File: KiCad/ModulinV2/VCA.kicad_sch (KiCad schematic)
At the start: 9 parts, among them IC12 AS3360D

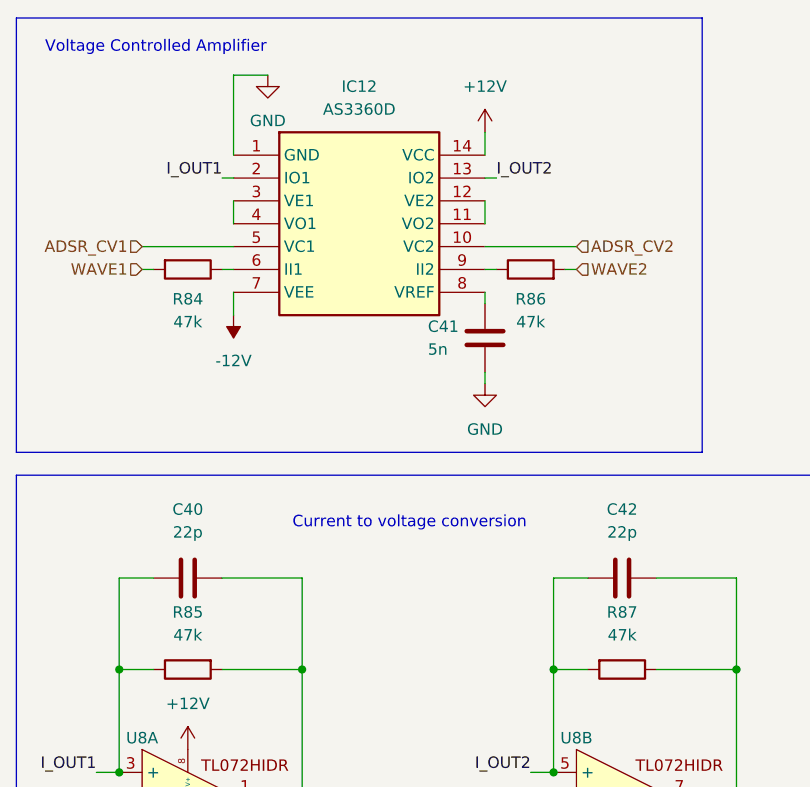
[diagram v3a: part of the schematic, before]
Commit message: Added initial power supply schematic and modified MCU components
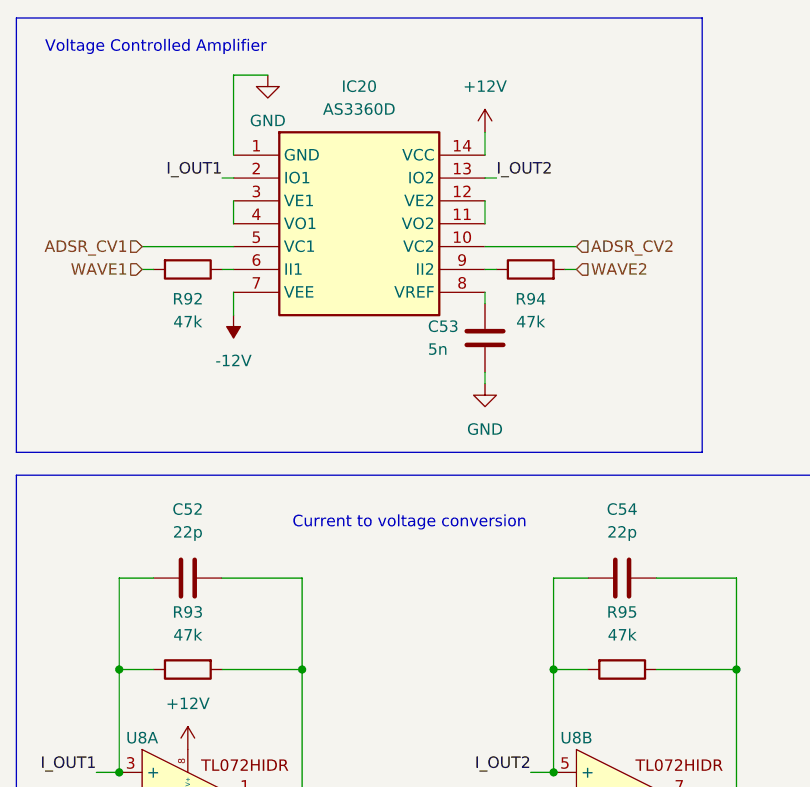
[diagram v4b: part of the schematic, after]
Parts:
- renumbered C40 to C52, C41 to C53, C42 to C54, IC12 to IC20, R84 to R92, R85 to R93, R86 to R94, R87 to R95
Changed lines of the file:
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@@
 		(dnp no)
 		(fields_autoplaced yes)
-		(property "Reference" "R87"
+		(property "Reference" "R95"
 			(at 81.28 80.01 90)
 			(effects
@@
 			(project "ModulinV2"
 				(path "/c6b34a57-3941-4b56-8b80-1848c7f41082/a5a8abcc-50bb-4382-96d0-cbdb724bb6e9"
-					(reference "R87")
+					(reference "R95")
 					(unit 1)
 				)
@@
 		(dnp no)
 		(fields_autoplaced yes)
-		(property "Reference" "#PWR0143"
+		(property "Reference" "#PWR0167"
 			(at 66.04 30.48 0)
 			(effects
@@
 			(project ""
 				(path "/c6b34a57-3941-4b56-8b80-1848c7f41082/a5a8abcc-50bb-4382-96d0-cbdb724bb6e9"
-					(reference "#PWR0143")
+					(reference "#PWR0167")
 					(unit 1)
 				)
@@
 		(on_board yes)
 		(dnp no)
-		(property "Reference" "R86"
+		(property "Reference" "R94"
 			(at 71.12 45.212 90)
 			(effects
@@
 			(project "ModulinV2"
 				(path "/c6b34a57-3941-4b56-8b80-1848c7f41082/a5a8abcc-50bb-4382-96d0-cbdb724bb6e9"
-					(reference "R86")
+					(reference "R94")
 					(unit 1)
 				)
@@
 		(dnp no)
 		(fields_autoplaced yes)
-		(property "Reference" "#PWR0139"
+		(property "Reference" "#PWR0163"
 			(at 33.02 99.06 0)
 			(effects
@@
 			(project "ModulinV2"
 				(path "/c6b34a57-3941-4b56-8b80-1848c7f41082/a5a8abcc-50bb-4382-96d0-cbdb724bb6e9"
-					(reference "#PWR0139")
+					(reference "#PWR0163")
 					(unit 1)
 				)
@@
 		(on_board yes)
 		(dnp no)
-		(property "Reference" "R84"
+		(property "Reference" "R92"
 			(at 33.02 45.212 90)
 			(effects
@@
 			(project "ModulinV2"
 				(path "/c6b34a57-3941-4b56-8b80-1848c7f41082/a5a8abcc-50bb-4382-96d0-cbdb724bb6e9"
-					(reference "R84")
+					(reference "R92")
 					(unit 1)
 				)
@@
 		(dnp no)
 		(fields_autoplaced yes)
-		(property "Reference" "#PWR0138"
+		(property "Reference" "#PWR0162"
 			(at 25.4 110.49 0)
 			(effects
@@
 			(project ""
 				(path "/c6b34a57-3941-4b56-8b80-1848c7f41082/a5a8abcc-50bb-4382-96d0-cbdb724bb6e9"
-					(reference "#PWR0138")
+					(reference "#PWR0162")
 					(unit 1)
 				)
@@
 		(dnp no)
 		(fields_autoplaced yes)
-		(property "Reference" "#PWR0144"
+		(property "Reference" "#PWR0168"
 			(at 66.04 60.96 0)
 			(effects
@@
 			(project ""
 				(path "/c6b34a57-3941-4b56-8b80-1848c7f41082/a5a8abcc-50bb-4382-96d0-cbdb724bb6e9"
-					(reference "#PWR0144")
+					(reference "#PWR0168")
 					(unit 1)
 				)
@@
 		(dnp no)
 		(fields_autoplaced yes)
-		(property "Reference" "#PWR0141"
+		(property "Reference" "#PWR0165"
 			(at 38.1 43.18 0)
 			(effects
@@
 			(project ""
 				(path "/c6b34a57-3941-4b56-8b80-1848c7f41082/a5a8abcc-50bb-4382-96d0-cbdb724bb6e9"
-					(reference "#PWR0141")
+					(reference "#PWR0165")
 					(unit 1)
 				)
@@
 		(dnp no)
 		(fields_autoplaced yes)
-		(property "Reference" "#PWR0142"
+		(property "Reference" "#PWR0166"
 			(at 41.91 26.67 0)
 			(effects
@@
 			(project ""
 				(path "/c6b34a57-3941-4b56-8b80-1848c7f41082/a5a8abcc-50bb-4382-96d0-cbdb724bb6e9"
-					(reference "#PWR0142")
+					(reference "#PWR0166")
 					(unit 1)
 				)
@@
 		(dnp no)
 		(fields_autoplaced yes)
-		(property "Reference" "R85"
+		(property "Reference" "R93"
 			(at 33.02 80.01 90)
 			(effects
@@
 			(project ""
 				(path "/c6b34a57-3941-4b56-8b80-1848c7f41082/a5a8abcc-50bb-4382-96d0-cbdb724bb6e9"
-					(reference "R85")
+					(reference "R93")
 					(unit 1)
 				)
@@
 		(dnp no)
 		(fields_autoplaced yes)
-		(property "Reference" "C40"
+		(property "Reference" "C52"
 			(at 33.02 68.58 90)
 			(effects
@@
 			(project ""
 				(path "/c6b34a57-3941-4b56-8b80-1848c7f41082/a5a8abcc-50bb-4382-96d0-cbdb724bb6e9"
-					(reference "C40")
+					(reference "C52")
 					(unit 1)
 				)
@@
 		(dnp no)
 		(fields_autoplaced yes)
-		(property "Reference" "#PWR0140"
+		(property "Reference" "#PWR0164"
 			(at 33.02 101.6 0)
 			(effects
@@
 			(project "ModulinV2"
 				(path "/c6b34a57-3941-4b56-8b80-1848c7f41082/a5a8abcc-50bb-4382-96d0-cbdb724bb6e9"
-					(reference "#PWR0140")
+					(reference "#PWR0164")
 					(unit 1)
 				)
@@
 		(dnp no)
 		(fields_autoplaced yes)
-		(property "Reference" "IC12"
+		(property "Reference" "IC20"
 			(at 52.07 21.59 0)
 			(effects
@@
 			(project ""
 				(path "/c6b34a57-3941-4b56-8b80-1848c7f41082/a5a8abcc-50bb-4382-96d0-cbdb724bb6e9"
-					(reference "IC12")
+					(reference "IC20")
 					(unit 1)
 				)
@@
 		(on_board yes)
 		(dnp no)
-		(property "Reference" "C41"
+		(property "Reference" "C53"
 			(at 59.69 48.26 0)
 			(effects
@@
 			(project ""
 				(path "/c6b34a57-3941-4b56-8b80-1848c7f41082/a5a8abcc-50bb-4382-96d0-cbdb724bb6e9"
-					(reference "C41")
+					(reference "C53")
 					(unit 1)
 				)
@@
 		(dnp no)
 		(fields_autoplaced yes)
-		(property "Reference" "#PWR0145"
+		(property "Reference" "#PWR0169"
 			(at 73.66 110.49 0)
 			(effects
@@
 			(project ""
 				(path "/c6b34a57-3941-4b56-8b80-1848c7f41082/a5a8abcc-50bb-4382-96d0-cbdb724bb6e9"
-					(reference "#PWR0145")
+					(reference "#PWR0169")
 					(unit 1)
 				)
@@
 		(dnp no)
 		(fields_autoplaced yes)
-		(property "Reference" "C42"
+		(property "Reference" "C54"
 			(at 81.28 68.58 90)
 			(effects
@@
 			(project ""
 				(path "/c6b34a57-3941-4b56-8b80-1848c7f41082/a5a8abcc-50bb-4382-96d0-cbdb724bb6e9"
-					(reference "C42")
-					(unit 1)
-				)
+					(reference "C54")
+					(unit 1)
+				)

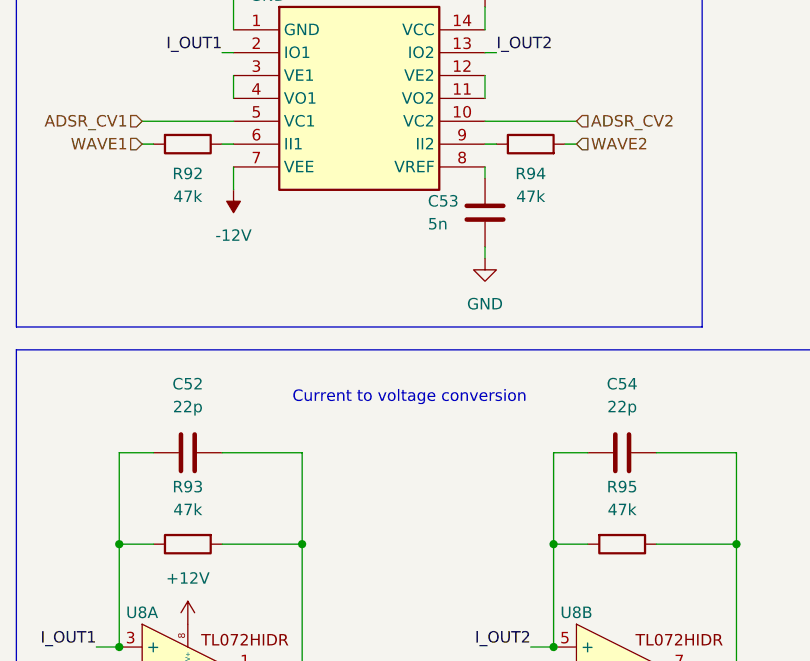
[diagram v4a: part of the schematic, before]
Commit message: Designed ADSR and better tuning schematics with digital/manual capability
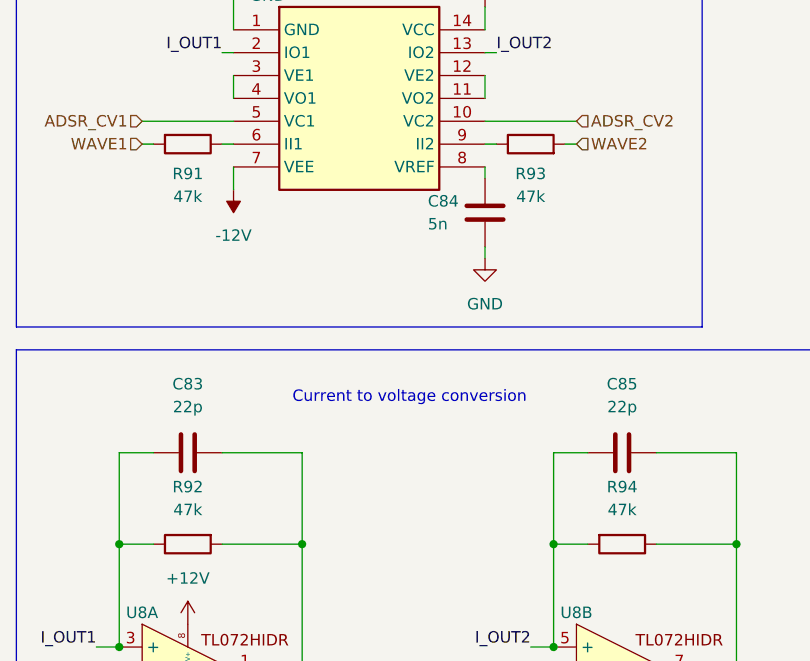
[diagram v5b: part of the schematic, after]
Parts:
- renumbered C52 to C83, C53 to C84, C54 to C85, R92 to R91, R93 to R92, R94 to R93, R95 to R94
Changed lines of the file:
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@@
 		(dnp no)
 		(fields_autoplaced yes)
-		(property "Reference" "R95"
+		(property "Reference" "R94"
 			(at 81.28 80.01 90)
 			(effects
@@
 			(project "ModulinV2"
 				(path "/c6b34a57-3941-4b56-8b80-1848c7f41082/a5a8abcc-50bb-4382-96d0-cbdb724bb6e9"
-					(reference "R95")
+					(reference "R94")
 					(unit 1)
 				)
@@
 		(dnp no)
 		(fields_autoplaced yes)
-		(property "Reference" "#PWR0167"
+		(property "Reference" "#PWR0201"
 			(at 66.04 30.48 0)
 			(effects
@@
 			(project ""
 				(path "/c6b34a57-3941-4b56-8b80-1848c7f41082/a5a8abcc-50bb-4382-96d0-cbdb724bb6e9"
-					(reference "#PWR0167")
+					(reference "#PWR0201")
 					(unit 1)
 				)
@@
 		(on_board yes)
 		(dnp no)
-		(property "Reference" "R94"
+		(property "Reference" "R93"
 			(at 71.12 45.212 90)
 			(effects
@@
 			(project "ModulinV2"
 				(path "/c6b34a57-3941-4b56-8b80-1848c7f41082/a5a8abcc-50bb-4382-96d0-cbdb724bb6e9"
-					(reference "R94")
+					(reference "R93")
 					(unit 1)
 				)
@@
 		(dnp no)
 		(fields_autoplaced yes)
-		(property "Reference" "#PWR0163"
+		(property "Reference" "#PWR0197"
 			(at 33.02 99.06 0)
 			(effects
@@
 			(project "ModulinV2"
 				(path "/c6b34a57-3941-4b56-8b80-1848c7f41082/a5a8abcc-50bb-4382-96d0-cbdb724bb6e9"
-					(reference "#PWR0163")
+					(reference "#PWR0197")
 					(unit 1)
 				)
@@
 		(on_board yes)
 		(dnp no)
-		(property "Reference" "R92"
+		(property "Reference" "R91"
 			(at 33.02 45.212 90)
 			(effects
@@
 			(project "ModulinV2"
 				(path "/c6b34a57-3941-4b56-8b80-1848c7f41082/a5a8abcc-50bb-4382-96d0-cbdb724bb6e9"
-					(reference "R92")
+					(reference "R91")
 					(unit 1)
 				)
@@
 		(dnp no)
 		(fields_autoplaced yes)
-		(property "Reference" "#PWR0162"
+		(property "Reference" "#PWR0196"
 			(at 25.4 110.49 0)
 			(effects
@@
 			(project ""
 				(path "/c6b34a57-3941-4b56-8b80-1848c7f41082/a5a8abcc-50bb-4382-96d0-cbdb724bb6e9"
-					(reference "#PWR0162")
+					(reference "#PWR0196")
 					(unit 1)
 				)
@@
 		(dnp no)
 		(fields_autoplaced yes)
-		(property "Reference" "#PWR0168"
+		(property "Reference" "#PWR0202"
 			(at 66.04 60.96 0)
 			(effects
@@
 			(project ""
 				(path "/c6b34a57-3941-4b56-8b80-1848c7f41082/a5a8abcc-50bb-4382-96d0-cbdb724bb6e9"
-					(reference "#PWR0168")
+					(reference "#PWR0202")
 					(unit 1)
 				)
@@
 		(dnp no)
 		(fields_autoplaced yes)
-		(property "Reference" "#PWR0165"
+		(property "Reference" "#PWR0199"
 			(at 38.1 43.18 0)
 			(effects
@@
 			(project ""
 				(path "/c6b34a57-3941-4b56-8b80-1848c7f41082/a5a8abcc-50bb-4382-96d0-cbdb724bb6e9"
-					(reference "#PWR0165")
+					(reference "#PWR0199")
 					(unit 1)
 				)
@@
 		(dnp no)
 		(fields_autoplaced yes)
-		(property "Reference" "#PWR0166"
+		(property "Reference" "#PWR0200"
 			(at 41.91 26.67 0)
 			(effects
@@
 			(project ""
 				(path "/c6b34a57-3941-4b56-8b80-1848c7f41082/a5a8abcc-50bb-4382-96d0-cbdb724bb6e9"
-					(reference "#PWR0166")
+					(reference "#PWR0200")
 					(unit 1)
 				)
@@
 		(dnp no)
 		(fields_autoplaced yes)
-		(property "Reference" "R93"
+		(property "Reference" "R92"
 			(at 33.02 80.01 90)
 			(effects
@@
 			(project ""
 				(path "/c6b34a57-3941-4b56-8b80-1848c7f41082/a5a8abcc-50bb-4382-96d0-cbdb724bb6e9"
-					(reference "R93")
+					(reference "R92")
 					(unit 1)
 				)
@@
 		(dnp no)
 		(fields_autoplaced yes)
-		(property "Reference" "C52"
+		(property "Reference" "C83"
 			(at 33.02 68.58 90)
 			(effects
@@
 			(project ""
 				(path "/c6b34a57-3941-4b56-8b80-1848c7f41082/a5a8abcc-50bb-4382-96d0-cbdb724bb6e9"
-					(reference "C52")
+					(reference "C83")
 					(unit 1)
 				)
@@
 		(dnp no)
 		(fields_autoplaced yes)
-		(property "Reference" "#PWR0164"
+		(property "Reference" "#PWR0198"
 			(at 33.02 101.6 0)
 			(effects
@@
 			(project "ModulinV2"
 				(path "/c6b34a57-3941-4b56-8b80-1848c7f41082/a5a8abcc-50bb-4382-96d0-cbdb724bb6e9"
-					(reference "#PWR0164")
+					(reference "#PWR0198")
 					(unit 1)
 				)
@@
 		(on_board yes)
 		(dnp no)
-		(property "Reference" "C53"
+		(property "Reference" "C84"
 			(at 59.69 48.26 0)
 			(effects
@@
 			(project ""
 				(path "/c6b34a57-3941-4b56-8b80-1848c7f41082/a5a8abcc-50bb-4382-96d0-cbdb724bb6e9"
-					(reference "C53")
+					(reference "C84")
 					(unit 1)
 				)
@@
 		(dnp no)
 		(fields_autoplaced yes)
-		(property "Reference" "#PWR0169"
+		(property "Reference" "#PWR0203"
 			(at 73.66 110.49 0)
 			(effects
@@
 			(project ""
 				(path "/c6b34a57-3941-4b56-8b80-1848c7f41082/a5a8abcc-50bb-4382-96d0-cbdb724bb6e9"
-					(reference "#PWR0169")
+					(reference "#PWR0203")
 					(unit 1)
 				)
@@
 		(dnp no)
 		(fields_autoplaced yes)
-		(property "Reference" "C54"
+		(property "Reference" "C85"
 			(at 81.28 68.58 90)
 			(effects
@@
 			(project ""
 				(path "/c6b34a57-3941-4b56-8b80-1848c7f41082/a5a8abcc-50bb-4382-96d0-cbdb724bb6e9"
-					(reference "C54")
-					(unit 1)
-				)
+					(reference "C85")
+					(unit 1)
+				)

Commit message: Added 4k7 pullups to I2C lines
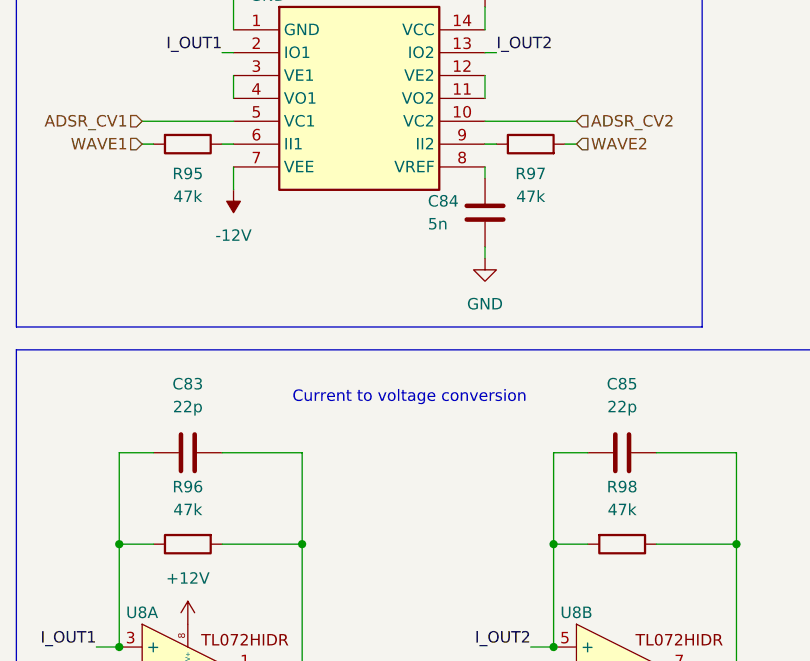
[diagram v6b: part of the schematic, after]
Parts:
- renumbered R91 to R95, R92 to R96, R93 to R97, R94 to R98
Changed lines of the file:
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@@
 		(dnp no)
 		(fields_autoplaced yes)
-		(property "Reference" "R94"
+		(property "Reference" "R98"
 			(at 81.28 80.01 90)
 			(effects
@@
 			(project "ModulinV2"
 				(path "/c6b34a57-3941-4b56-8b80-1848c7f41082/a5a8abcc-50bb-4382-96d0-cbdb724bb6e9"
-					(reference "R94")
+					(reference "R98")
 					(unit 1)
 				)
@@
 		(dnp no)
 		(fields_autoplaced yes)
-		(property "Reference" "#PWR0201"
+		(property "Reference" "#PWR0196"
 			(at 66.04 30.48 0)
 			(effects
@@
 			(project ""
 				(path "/c6b34a57-3941-4b56-8b80-1848c7f41082/a5a8abcc-50bb-4382-96d0-cbdb724bb6e9"
-					(reference "#PWR0201")
+					(reference "#PWR0196")
 					(unit 1)
 				)
@@
 		(on_board yes)
 		(dnp no)
-		(property "Reference" "R93"
+		(property "Reference" "R97"
 			(at 71.12 45.212 90)
 			(effects
@@
 			(project "ModulinV2"
 				(path "/c6b34a57-3941-4b56-8b80-1848c7f41082/a5a8abcc-50bb-4382-96d0-cbdb724bb6e9"
-					(reference "R93")
+					(reference "R97")
 					(unit 1)
 				)
@@
 		(dnp no)
 		(fields_autoplaced yes)
-		(property "Reference" "#PWR0197"
+		(property "Reference" "#PWR0192"
 			(at 33.02 99.06 0)
 			(effects
@@
 			(project "ModulinV2"
 				(path "/c6b34a57-3941-4b56-8b80-1848c7f41082/a5a8abcc-50bb-4382-96d0-cbdb724bb6e9"
-					(reference "#PWR0197")
+					(reference "#PWR0192")
 					(unit 1)
 				)
@@
 		(on_board yes)
 		(dnp no)
-		(property "Reference" "R91"
+		(property "Reference" "R95"
 			(at 33.02 45.212 90)
 			(effects
@@
 			(project "ModulinV2"
 				(path "/c6b34a57-3941-4b56-8b80-1848c7f41082/a5a8abcc-50bb-4382-96d0-cbdb724bb6e9"
-					(reference "R91")
+					(reference "R95")
 					(unit 1)
 				)
@@
 		(dnp no)
 		(fields_autoplaced yes)
-		(property "Reference" "#PWR0196"
+		(property "Reference" "#PWR0191"
 			(at 25.4 110.49 0)
 			(effects
@@
 			(project ""
 				(path "/c6b34a57-3941-4b56-8b80-1848c7f41082/a5a8abcc-50bb-4382-96d0-cbdb724bb6e9"
-					(reference "#PWR0196")
+					(reference "#PWR0191")
 					(unit 1)
 				)
@@
 		(dnp no)
 		(fields_autoplaced yes)
-		(property "Reference" "#PWR0202"
+		(property "Reference" "#PWR0197"
 			(at 66.04 60.96 0)
 			(effects
@@
 			(project ""
 				(path "/c6b34a57-3941-4b56-8b80-1848c7f41082/a5a8abcc-50bb-4382-96d0-cbdb724bb6e9"
-					(reference "#PWR0202")
+					(reference "#PWR0197")
 					(unit 1)
 				)
@@
 		(dnp no)
 		(fields_autoplaced yes)
-		(property "Reference" "#PWR0199"
+		(property "Reference" "#PWR0194"
 			(at 38.1 43.18 0)
 			(effects
@@
 			(project ""
 				(path "/c6b34a57-3941-4b56-8b80-1848c7f41082/a5a8abcc-50bb-4382-96d0-cbdb724bb6e9"
-					(reference "#PWR0199")
+					(reference "#PWR0194")
 					(unit 1)
 				)
@@
 		(dnp no)
 		(fields_autoplaced yes)
-		(property "Reference" "#PWR0200"
+		(property "Reference" "#PWR0195"
 			(at 41.91 26.67 0)
 			(effects
@@
 			(project ""
 				(path "/c6b34a57-3941-4b56-8b80-1848c7f41082/a5a8abcc-50bb-4382-96d0-cbdb724bb6e9"
-					(reference "#PWR0200")
+					(reference "#PWR0195")
 					(unit 1)
 				)
@@
 		(dnp no)
 		(fields_autoplaced yes)
-		(property "Reference" "R92"
+		(property "Reference" "R96"
 			(at 33.02 80.01 90)
 			(effects
@@
 			(project ""
 				(path "/c6b34a57-3941-4b56-8b80-1848c7f41082/a5a8abcc-50bb-4382-96d0-cbdb724bb6e9"
-					(reference "R92")
+					(reference "R96")
 					(unit 1)
 				)
@@
 		(dnp no)
 		(fields_autoplaced yes)
-		(property "Reference" "#PWR0198"
+		(property "Reference" "#PWR0193"
 			(at 33.02 101.6 0)
 			(effects
@@
 			(project "ModulinV2"
 				(path "/c6b34a57-3941-4b56-8b80-1848c7f41082/a5a8abcc-50bb-4382-96d0-cbdb724bb6e9"
-					(reference "#PWR0198")
+					(reference "#PWR0193")
 					(unit 1)
 				)
@@
 		(dnp no)
 		(fields_autoplaced yes)
-		(property "Reference" "#PWR0203"
+		(property "Reference" "#PWR0198"
 			(at 73.66 110.49 0)
 			(effects
@@
 			(project ""
 				(path "/c6b34a57-3941-4b56-8b80-1848c7f41082/a5a8abcc-50bb-4382-96d0-cbdb724bb6e9"
-					(reference "#PWR0203")
-					(unit 1)
-				)
+					(reference "#PWR0198")
+					(unit 1)
+				)

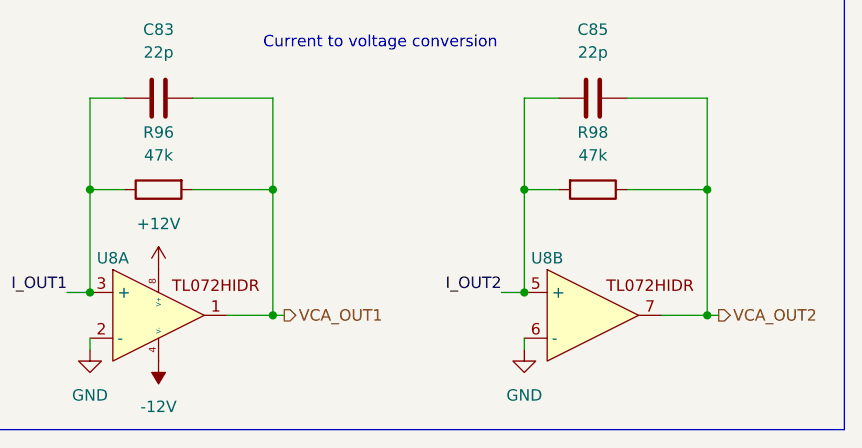
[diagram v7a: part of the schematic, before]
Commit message: Updated TL074 and 72 symbols
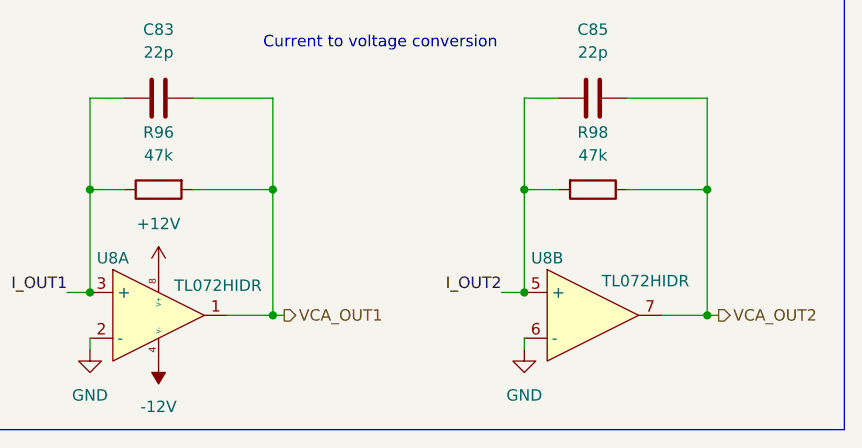
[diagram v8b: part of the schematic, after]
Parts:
- U8: value ~ -> TL072HIDR
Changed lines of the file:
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@@
 			)
 		)
-		(property "Value" "~"
-			(at 84.4955 93.98 0)
+		(property "Value" "TL072HIDR"
+			(at 87.122 96.52 0)
 			(effects
 				(font
@@
 			)
 		)
-		(property "Value" "~"
-			(at 45.72 97.0849 0)
-			(effects
-				(font
+		(property "Value" "TL072HIDR"
+			(at 39.624 97.028 0)
+			(effects
+				(font
